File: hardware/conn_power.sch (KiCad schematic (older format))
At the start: 20 parts

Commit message: more work on tdr schematic
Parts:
- U?: symbol synth_lib:FT2232H -> tdr-rescue:FT2232H-synth_lib
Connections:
- net labels added: ANALOG_TRIG
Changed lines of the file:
@@
 $EndComp
 $Comp
-L synth_lib:FT2232H U?
+L tdr-rescue:FT2232H-synth_lib U?
 U 1 1 5BCAC7E0
 P 4050 6950
@@
 Wire Wire Line
 	3550 9250 3650 9250
+Text HLabel 10200 8550 0    50   Input ~ 0
+ANALOG_TRIG
 $EndSCHEMATC

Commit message: work on tdr schematic..
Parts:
- removed J?: USB_B_Micro, symbol Connector:USB_B_Micro
- removed U?: FT2232H, symbol tdr-rescue:FT2232H-synth_lib
- added C? (x12): 2.2 uF, symbol Device:C_Small
- added C?: 1 uF, symbol Device:C_Small
- added J? (x2): Conn_Coaxial, symbol Connector:Conn_Coaxial
- added R? (x12): TBD, symbol Device:R_Small
- added R? (x2): R_Small, symbol Device:R_Small
- added R? (x7): 10k, symbol Device:R_Small
- added R? (x2): JMP, symbol Device:R_Small
- added R?: DNP, symbol Device:R_Small
- added U? (x4): LD39100, symbol ld39100:LD39100
- added U?: LM27762, symbol lm27762:LM27762
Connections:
- net labels added: +1V35, PGOOD_2V5, ~PGOOD
- wire segments 68 -> 194
- no-connect marks 17 -> 0
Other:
- note added: "TODO: GATE OFF PGOOD FROM OTHER RAIL"
- note removed: "NC?"
- moved on the sheet: J?, R?

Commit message: footprint assignment
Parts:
- added C214: 100 uF, Capacitors_SMD:c_elec_6.3x5.8, symbol Device:CP1_Small
- added C215: 100 nF, Capacitors_SMD:C_0402, symbol Device:C_Small
- added D201: RED, LEDs:LED_0603, symbol Device:LED
- added D202: TBD, Diodes_SMD:SOD-123, symbol Device:D_Small
- added F201: Polyfuse_Small, Resistors_SMD:R_1210, symbol Device:Polyfuse_Small
- added L201: L_Small, Resistors_SMD:R_1210, symbol Device:L_Small
- added R235: 10k, Resistors_SMD:R_0402, symbol Device:R_Small
- C201, C202, C203, C204, C205, C206, C208, C209, C210, C211, C212, C213: renamed from C?; footprint (none) -> Capacitors_SMD:C_0603
- C207: renamed from C?; footprint (none) -> Capacitors_SMD:C_0402
- J201: renamed from J?; footprint (none) -> Terminal_Blocks:TerminalBlock_Pheonix_MPT-2.54mm_2pol
- J202, J203, J204, J205, J207: renamed from J?; footprint (none) -> vna_footprints:SF2921-61345
- J206, J208, J209: renamed from J?; footprint (none) -> vna_footprints:732511150_sma_thin
- J210: renamed from J?; footprint (none) -> vna_footprints:BARREL_JACK
- R201, R202, R203, R204, R205, R206, R207, R208, R209, R210, R211, R212, R213, R214, R215, R216, R217, R218, R219, R220, R221, R222, R223, R224, R225, R226, R227, R228, R229, R230, R231, R232, R233, R234: renamed from R?; footprint (none) -> Resistors_SMD:R_0402
- U201, U202, U203, U204: renamed from U?; footprint (none) -> Housings_DFN_QFN:DFN-6-1EP_3x3mm_Pitch0.95mm
- U205: renamed from U?; footprint (none) -> vna_footprints:WSON-12-1EP_3x2mm_Pitch0.5mm
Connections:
- wire segments 194 -> 209
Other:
- moved on the sheet: C203, C204, C205, C206, C207, C208, C209, C210, C211, C212, C213, J201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

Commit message: work on schematic..
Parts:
- removed C203, C204, C208, C210: 2.2 uF, Capacitors_SMD:C_0603, symbol Device:C_Small
- removed R206: TBD, Resistors_SMD:R_0402, symbol Device:R_Small
- removed U202, U204: LD39100, Housings_DFN_QFN:DFN-6-1EP_3x3mm_Pitch0.95mm, symbol ld39100:LD39100
- added Q201: SI2369DS, TO_SOT_Packages_SMD:SOT-23, symbol Device:Q_PMOS_GSD
- added R236, R237: DNP, Resistors_SMD:R_0402, symbol Device:R_Small
- R202: value 10k -> JMP
- R204: value TBD -> JMP
- R207, R209, R210: value 10k -> DNP
- R213, R215: value TBD -> DNP
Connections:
- net labels added: PGOOD_1V35, PGOOD_3V3, ~PGOOD_5V
- net labels removed: +2V5, +3.3VP, PGOOD_2V5, ~PGOOD
- wire segments 209 -> 187
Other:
- note added: "PGOOD NEEDS EXTERNAL PULLUP, PULLED LOW IF BELOW 0.8 * NOMINAL VOUT"
- moved on the sheet: C205, C206, C207, C209, C211, C212, C213, C214, C215, D201, D202, F201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

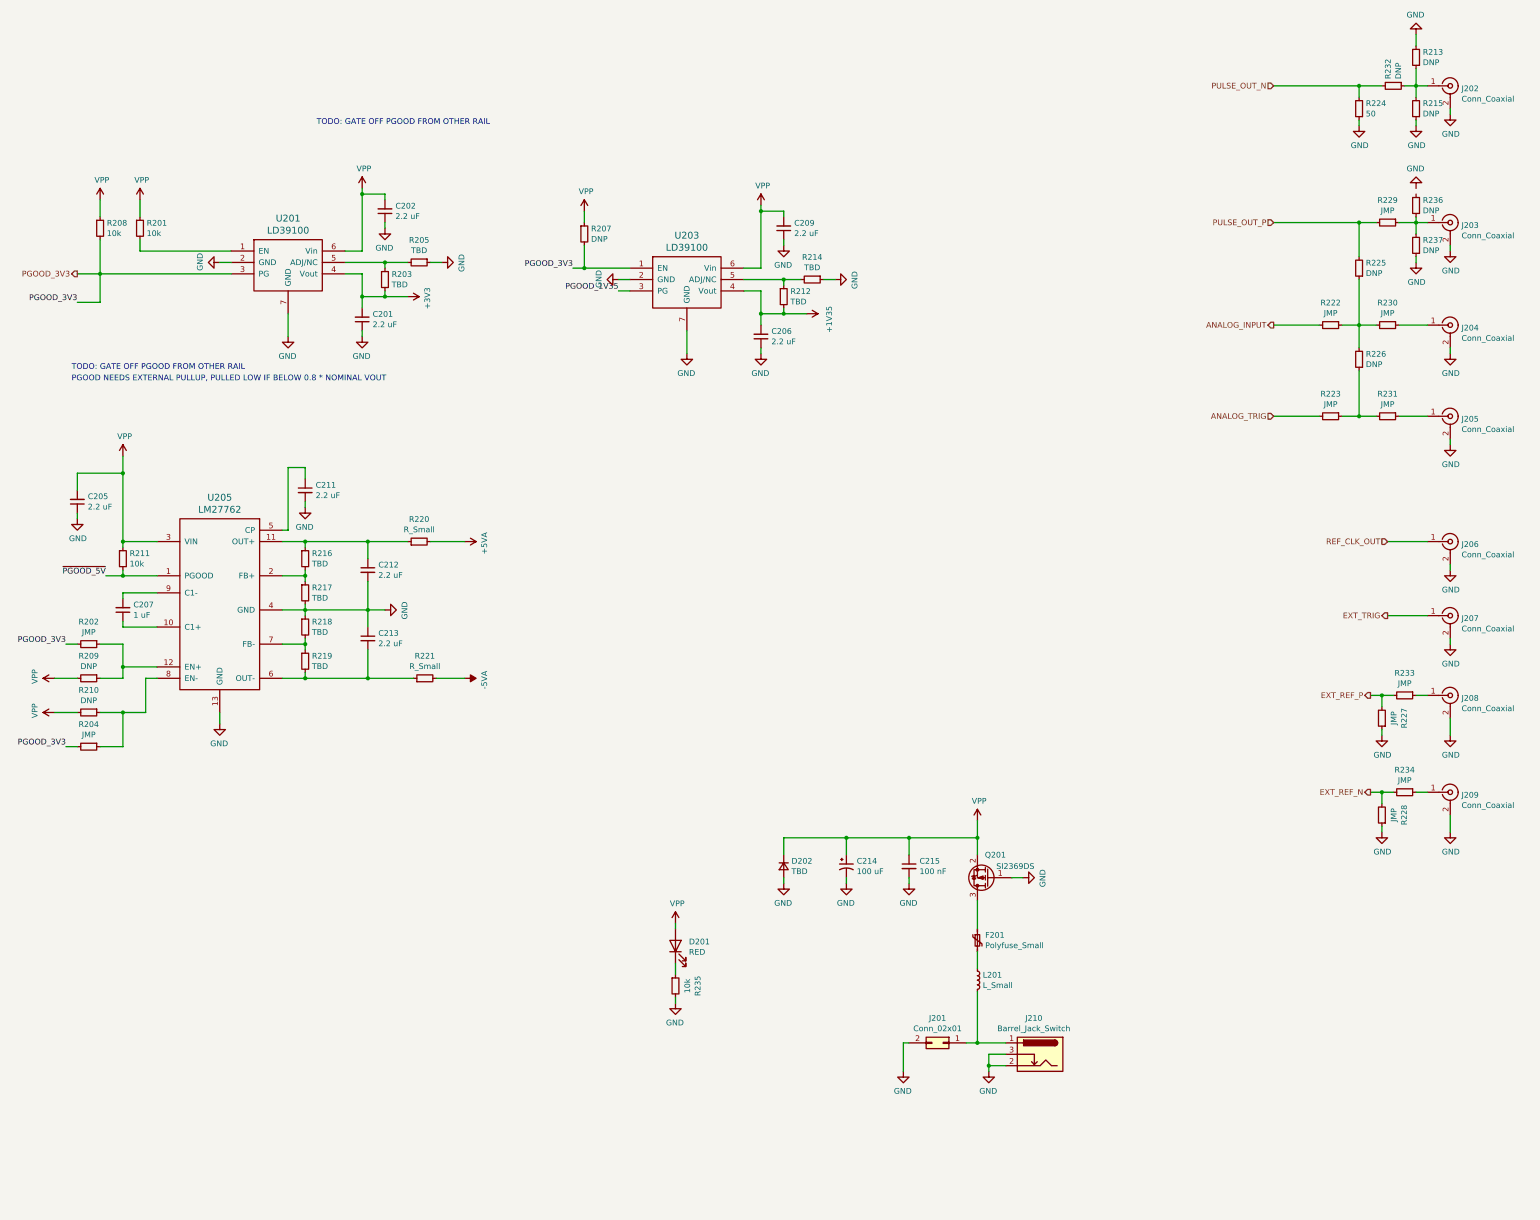
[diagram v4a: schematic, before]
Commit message: work on tdr component placement
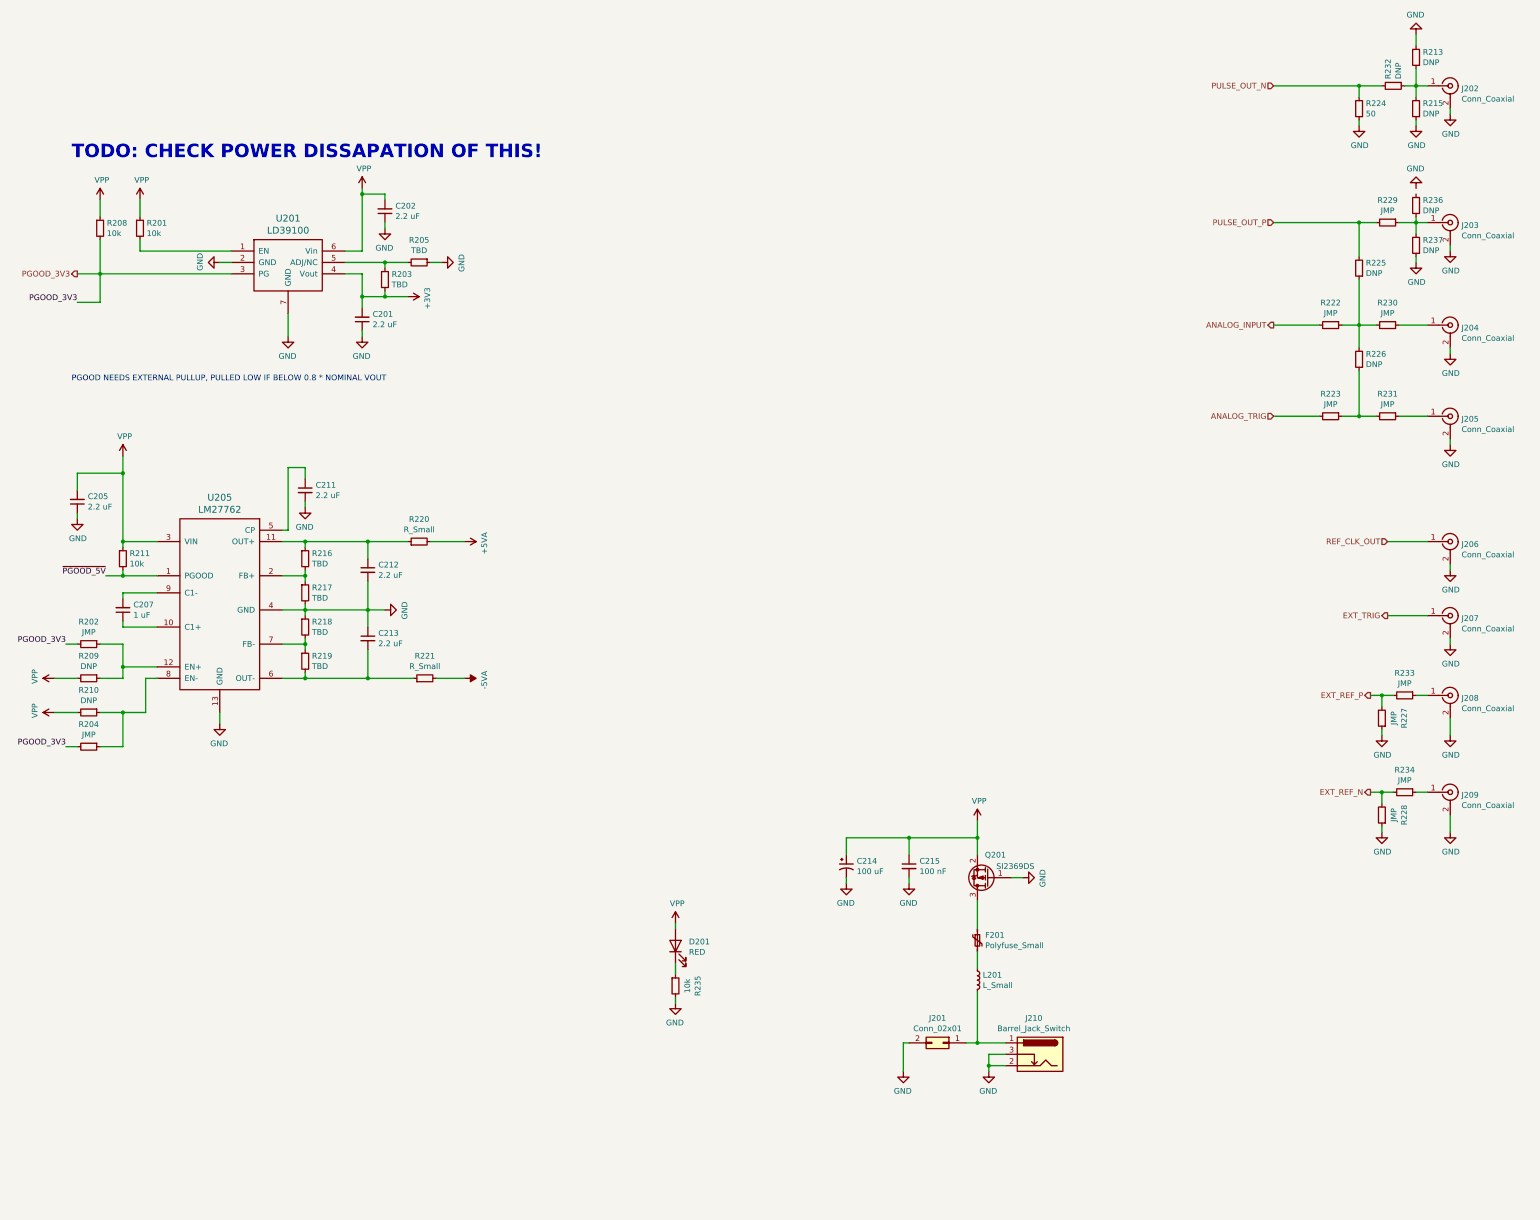
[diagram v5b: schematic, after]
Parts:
- removed C206, C209: 2.2 uF, Capacitors_SMD:C_0603, symbol Device:C_Small
- removed D202: TBD, Diodes_SMD:SOD-123, symbol Device:D_Small
- removed R207: DNP, Resistors_SMD:R_0402, symbol Device:R_Small
- removed R212, R214: TBD, Resistors_SMD:R_0402, symbol Device:R_Small
- removed U203: LD39100, Housings_DFN_QFN:DFN-6-1EP_3x3mm_Pitch0.95mm, symbol ld39100:LD39100
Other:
- note added: "TODO: CHECK POWER DISSAPATION OF THIS!"
- note removed: "TODO: GATE OFF PGOOD FROM OTHER RAIL"

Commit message: more component placement on tdr..
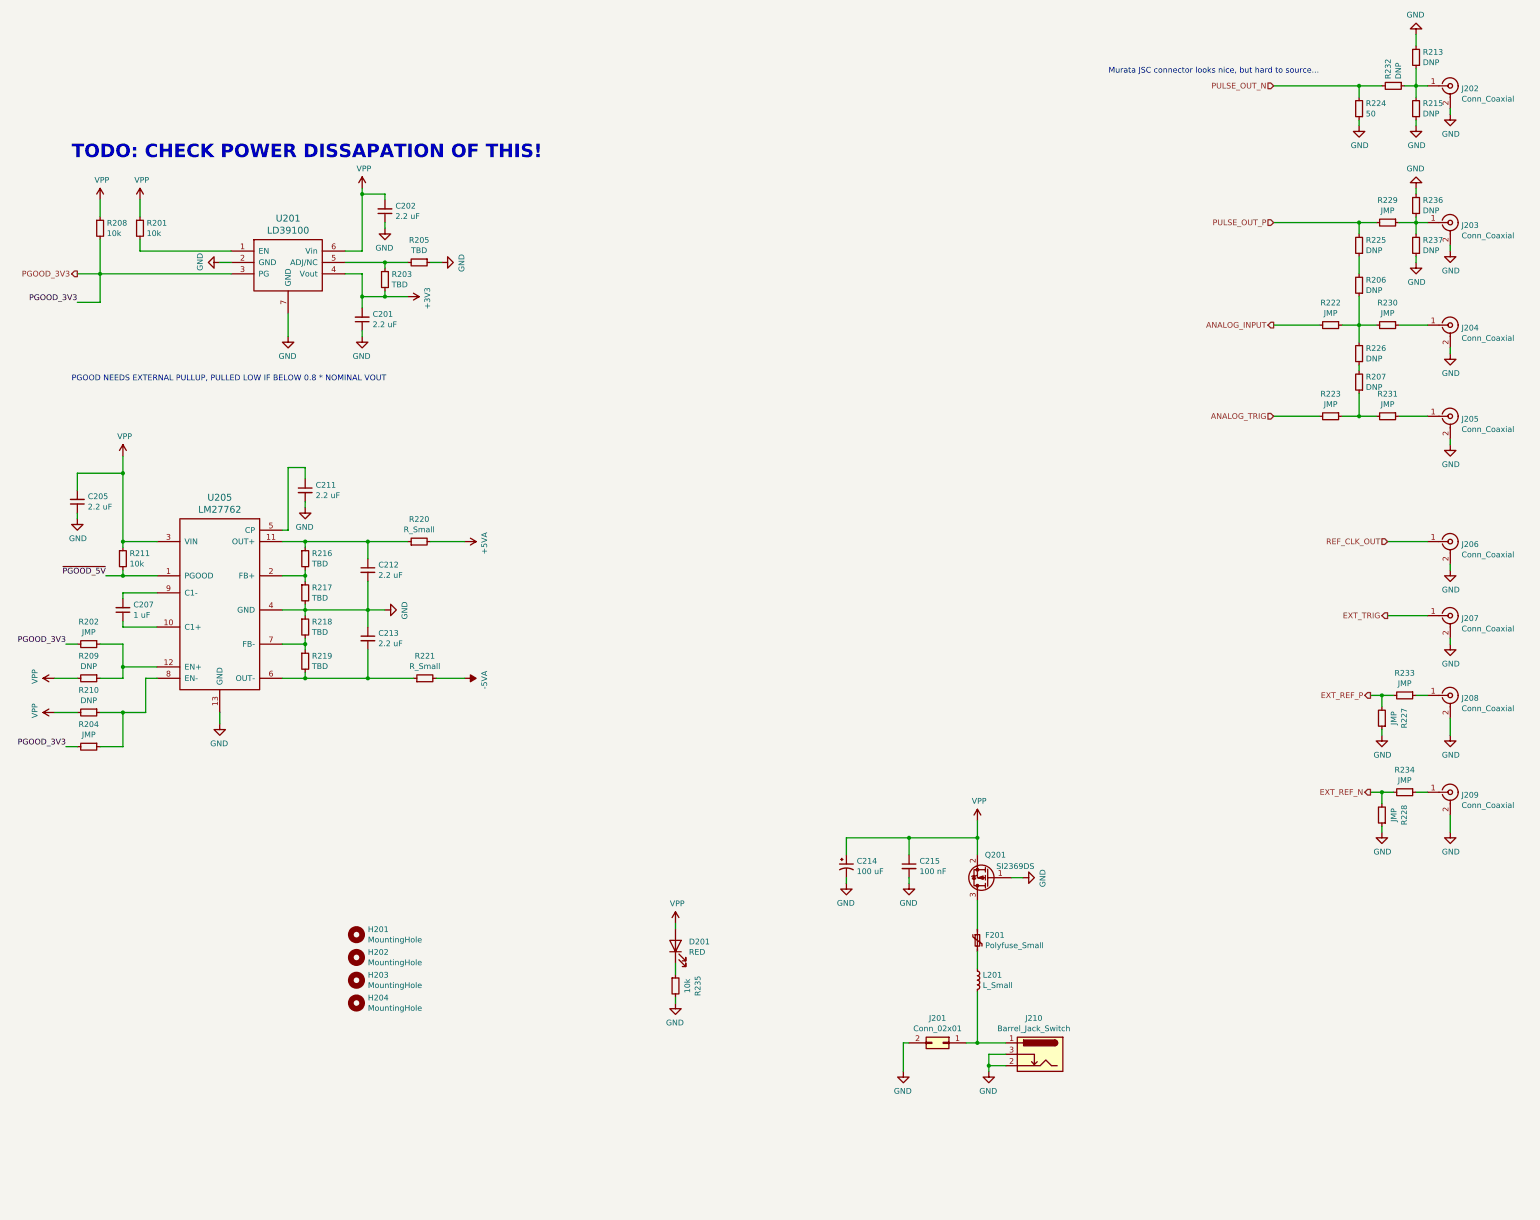
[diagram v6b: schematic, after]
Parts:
- added H201, H202, H203, H204: MountingHole, Mounting_Holes:MountingHole_2-5mm, symbol Mechanical:MountingHole
- added R206, R207: DNP, Resistors_SMD:R_0402, symbol Device:R_Small
- J202: footprint vna_footprints:SF2921-61345 -> vna_footprints:734120110_ufl_umc
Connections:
- net GND: now also R236.2
- net at R222.1, R226.2, R230.2: now also R206.1; no longer R225.1
- net at R223.1, R231.2: now also R207.1; no longer R226.1
- new net: R206.2, R225.1
- new net: R207.2, R226.1
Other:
- note added: "Murata JSC connector looks nice, but hard to source..."
- moved on the sheet: R225, R226
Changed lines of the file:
@@
 L Device:R_Small R225
 U 1 1 5BC3BF6B
-P 14250 2700
-F 0 "R225" H 14191 2654 50  0000 R CNN
-F 1 "DNP" H 14191 2745 50  0000 R CNN
-F 2 "Resistors_SMD:R_0402" H 14250 2700 50  0001 C CNN
-F 3 "~" H 14250 2700 50  0001 C CNN
-	1    14250 2700
+P 14250 2500
+F 0 "R225" H 14191 2454 50  0000 R CNN
+F 1 "DNP" H 14191 2545 50  0000 R CNN
+F 2 "Resistors_SMD:R_0402" H 14250 2500 50  0001 C CNN
+F 3 "~" H 14250 2500 50  0001 C CNN
+	1    14250 2500
 	-1   0    0    1
 $EndComp
@@
 Wire Wire Line
 	14400 3200 14250 3200
-Wire Wire Line
-	14250 3200 14250 2800
 Connection ~ 14250 3200
 Wire Wire Line
 	14250 3200 14100 3200
 Wire Wire Line
-	14250 2600 14250 2300
-Wire Wire Line
-	14250 2300 14400 2300
-Wire Wire Line
 	14600 2300 14750 2300
-Wire Wire Line
-	14250 2300 13500 2300
-Connection ~ 14250 2300
 Wire Wire Line
 	13900 3200 13500 3200
@@
 F 0 "J202" H 15149 1076 50  0000 L CNN
 F 1 "Conn_Coaxial" H 15149 985 50  0000 L CNN
-F 2 "vna_footprints:SF2921-61345" H 15050 1100 50  0001 C CNN
+F 2 "vna_footprints:734120110_ufl_umc" H 15050 1100 50  0001 C CNN
 F 3 " ~" H 15050 1100 50  0001 C CNN
 	1    15050 1100
@@
 $EndComp
 Wire Wire Line
-	14400 4000 14250 4000
-Wire Wire Line
-	14250 4000 14250 3600
-Connection ~ 14250 4000
-Wire Wire Line
-	14250 4000 14100 4000
-Wire Wire Line
 	13900 4000 13500 4000
 $Comp
 L Device:R_Small R226
 U 1 1 5C206702
-P 14250 3500
-F 0 "R226" H 14191 3454 50  0000 R CNN
-F 1 "DNP" H 14191 3545 50  0000 R CNN
-F 2 "Resistors_SMD:R_0402" H 14250 3500 50  0001 C CNN
-F 3 "~" H 14250 3500 50  0001 C CNN
-	1    14250 3500
+P 14250 3450
+F 0 "R226" H 14191 3404 50  0000 R CNN
+F 1 "DNP" H 14191 3495 50  0000 R CNN
+F 2 "Resistors_SMD:R_0402" H 14250 3450 50  0001 C CNN
+F 3 "~" H 14250 3450 50  0001 C CNN
+	1    14250 3450
 	-1   0    0    1
 $EndComp
 Wire Wire Line
 	14600 4000 14850 4000
-Wire Wire Line
-	14250 3400 14250 3200
 $Comp
 L Device:CP1_Small C214
@@
 Text Notes 2950 1750 0    118  ~ 24
 TODO: CHECK POWER DISSAPATION OF THIS!
+Wire Wire Line
+	14750 2050 14750 2000
+Wire Wire Line
+	14100 4000 14250 4000
+$Comp
+L Device:R_Small R207
+U 1 1 5C2AD4A3
+P 14250 3700
+F 0 "R207" H 14191 3654 50  0000 R CNN
+F 1 "DNP" H 14191 3745 50  0000 R CNN
+F 2 "Resistors_SMD:R_0402" H 14250 3700 50  0001 C CNN
+F 3 "~" H 14250 3700 50  0001 C CNN
+	1    14250 3700
+	-1   0    0    1
+$EndComp
+Wire Wire Line
+	14250 3800 14250 4000
+Connection ~ 14250 4000
+Wire Wire Line
+	14250 4000 14400 4000
+Wire Wire Line
+	14250 3600 14250 3550
+Wire Wire Line
+	14250 3350 14250 3200
+Wire Wire Line
+	13500 2300 14250 2300
+$Comp
+L Device:R_Small R206
+U 1 1 5C2CAA43
+P 14250 2850
+F 0 "R206" H 14191 2804 50  0000 R CNN
+F 1 "DNP" H 14191 2895 50  0000 R CNN
+F 2 "Resistors_SMD:R_0402" H 14250 2850 50  0001 C CNN
+F 3 "~" H 14250 2850 50  0001 C CNN
+	1    14250 2850
+	-1   0    0    1
+$EndComp
+Wire Wire Line
+	14250 2950 14250 3200
+Wire Wire Line
+	14250 2750 14250 2600
+Wire Wire Line
+	14250 2400 14250 2300
+Connection ~ 14250 2300
+Wire Wire Line
+	14250 2300 14400 2300
+$Comp
+L Mechanical:MountingHole H201
+U 1 1 5C2E3428
+P 5450 8550
+F 0 "H201" H 5550 8596 50  0000 L CNN
+F 1 "MountingHole" H 5550 8505 50  0000 L CNN
+F 2 "Mounting_Holes:MountingHole_2-5mm" H 5450 8550 50  0001 C CNN
+F 3 "~" H 5450 8550 50  0001 C CNN
+	1    5450 8550
+	1    0    0    -1
+$EndComp
+$Comp
+L Mechanical:MountingHole H202
+U 1 1 5C2E35F0
+P 5450 8750
+F 0 "H202" H 5550 8796 50  0000 L CNN
+F 1 "MountingHole" H 5550 8705 50  0000 L CNN
+F 2 "Mounting_Holes:MountingHole_2-5mm" H 5450 8750 50  0001 C CNN
+F 3 "~" H 5450 8750 50  0001 C CNN
+	1    5450 8750
+	1    0    0    -1
+$EndComp
+$Comp
+L Mechanical:MountingHole H203
+U 1 1 5C2E3686
+P 5450 8950
+F 0 "H203" H 5550 8996 50  0000 L CNN
+F 1 "MountingHole" H 5550 8905 50  0000 L CNN
+F 2 "Mounting_Holes:MountingHole_2-5mm" H 5450 8950 50  0001 C CNN
+F 3 "~" H 5450 8950 50  0001 C CNN
+	1    5450 8950
+	1    0    0    -1
+$EndComp
+$Comp
+L Mechanical:MountingHole H204
+U 1 1 5C2E3734
+P 5450 9150
+F 0 "H204" H 5550 9196 50  0000 L CNN
+F 1 "MountingHole" H 5550 9105 50  0000 L CNN
+F 2 "Mounting_Holes:MountingHole_2-5mm" H 5450 9150 50  0001 C CNN
+F 3 "~" H 5450 9150 50  0001 C CNN
+	1    5450 9150
+	1    0    0    -1
+$EndComp
+Text Notes 12050 1000 0    50   ~ 0
+Murata JSC connector looks nice, but hard to source...
 $EndSCHEMATC
